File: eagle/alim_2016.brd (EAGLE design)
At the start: 160 x 100 mm, 22 parts, among them J1 AVR_SPI_PRG_6PTH, J2 AVR_SPI_PRG_6PTH, U1 3.3V, U2 LM2678S-5.0, U3 ATMEGA328P, U4 LM2596S-ADJ, U5 ATTINY85-20SU

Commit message: thermal vias
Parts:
- added 12V: 1751248, con-phoenix-350:1751248
- added R2, R3, R4, R5: 10K, resistor:M0805
- added S1, S2: (no value), SparkFun-Electromechanical:TACTILE-PTH
- moved J2 169.1 mm to (144.5, 48.6)
- moved U5 158.2 mm to (147.0, 44.1), turned to 180 degrees
- moved 24V 115.1 mm to (53.0, 29.8), turned to 0 degrees
- moved 8V 91.9 mm to (74.0, 29.8), turned to 0 degrees
- moved 5V 77.4 mm to (84.8, 29.8), turned to 0 degrees
- moved 3.3V 63.0 mm to (95.6, 29.8), turned to 0 degrees
- moved C2 57.3 mm to (88.6, 39.4), turned to 180 degrees
- moved U$20 56.8 mm to (40.6, 32.4), turned to 270 degrees
- moved U1 49.2 mm to (96.2, 40.0), turned to 180 degrees
- moved C3 48.7 mm to (51.8, 46.7), turned to 0 degrees
- moved C1 48.7 mm to (88.6, 47.6), turned to 180 degrees
- moved Q1 46.9 mm to (47.9, 43.2), turned to 0 degrees
- moved J1 43.3 mm to (48.6, 49.5)
- moved BAT1 42.5 mm to (13.3, 32.4)
- moved BAT2 42.5 mm to (13.3, 45.1)
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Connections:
- removed net N$38: 24V.1, U$20.3
- new net BAT24_CUT: R2.1, S2.3, U$20.1, U3.32
- new net N$12: 24V.1, BAT2.1, R3.1
- new net N$13: BAT3.2, R5.2, U$19.3
- new net N$15: R5.1, S1.1, U$19.1
- net 12V: now also 12V.1, BAT3.1, S1.3, U2.2; no longer U$19.3
- net GND: now also 12V.2, U$19.TAB, U$20.TAB; no longer BAT1.2, BAT3.2
- net N$8: now also BAT1.2, R2.2, R4.2, U$20.3; no longer BAT2.1, U$20.TAB
- net N$9: now also R3.2, R4.1, S2.1; no longer BAT3.1, U$19.TAB
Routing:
- net 12V: track 0.00 -> 163.2 mm, vias 0 -> 1
- net N$12: track 0.00 -> 59.7 mm
- net N$13: track 0.00 -> 18.3 mm
- net BAT24_CUT: track 0.00 -> 14.6 mm
- net N$42: track 0.00 -> 8.57 mm
- net N$40: track 0.00 -> 7.67 mm
- net N$41: track 0.00 -> 7.30 mm
- net N$8: track 14.9 -> 22.0 mm
- net 5.0V: track 40.6 -> 33.7 mm, vias 1 -> 3
- net N$6: track 12.6 -> 19.3 mm, vias 0 -> 1
- net N$39: track 0.00 -> 6.23 mm
- net N$15: track 0.00 -> 5.34 mm
- net N$2: track 13.3 -> 8.16 mm
- net RESET: track 19.0 -> 22.3 mm, vias 1 -> 2
- net N$3: track 5.67 -> 8.72 mm
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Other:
- board size 160 x 100 mm -> 160 x 67 mm

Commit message: pcb rearranging
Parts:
- removed U3: ATMEGA328P, SparkFun-DigitalIC:TQFP32-08
- added D1, D2: (no value), alim:SOD-123
- added LED1, LED4, LED7, LED8: RED, microbuilder:CHIPLED_0805_NOOUTLINE
- added LED2, LED5: YELLOW, microbuilder:CHIPLED_0805_NOOUTLINE
- added LED3, LED6: GREEN, microbuilder:CHIPLED_0805_NOOUTLINE
- added R10, R11, R12, R13, R6, R8, R9: 1K, resistor:M0805
- added R7: 220, resistor:M0805
- added U6: ATMEGA328P_TQFP, SparkFun-DigitalIC:TQFP32-08
- R3: value 10K -> 1K
- R4: value 10K -> 220
- S1, S2: value (none) -> SWITCH-MOMENTARY-2PTH
- moved C4 29.3 mm to (61.0, 17.8)
- moved Q1 29.3 mm to (67.0, 21.0)
- moved R1 29.3 mm to (47.0, 23.2)
- moved J1 29.3 mm to (67.6, 27.3)
- moved C3 29.3 mm to (70.8, 24.4)
- moved R4 18.3 mm to (32.7, 49.2), turned to 90 degrees
- moved 3.3V 11.2 mm to (96.8, 41.0)
- moved 5V 11.2 mm to (86.0, 41.0)
- moved C2 11.2 mm to (89.9, 50.5)
- moved 12V 11.2 mm to (64.8, 41.0)
- moved 24V 11.2 mm to (54.3, 41.0)
- moved 8V 11.2 mm to (75.2, 41.0)
- moved BAT1 11.2 mm to (14.6, 43.5)
- moved R2 11.2 mm to (31.1, 43.5)
- moved S1 11.2 mm to (25.4, 67.0)
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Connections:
- new net BAT12_CUT: D2.C, R5.1, R6.2, R7.1, S1.1, U$19.1
- new net N$10: LED7.A, R6.1
- new net N$11: R4.2, U6.32
- new net N$14: R7.2, U6.24
- new net N$16: LED5.A, R9.1
- new net N$17: LED6.A, R10.1
- new net N$18: LED1.A, R11.1
- new net N$19: LED2.A, R12.1
- new net N$20: LED3.A, R13.1
- net 5.0V: now also U6.4, U6.6; no longer U3.4, U3.6
- net BAT24_CUT: now also D1.C, R3.2, R4.1; no longer U3.32
- net GND: now also D1.A, D2.A, LED1.C, LED2.C, LED3.C, LED4.C, LED5.C, LED6.C, LED7.C, LED8.C, U6.3, U6.5; no longer U3.3, U3.5
- net N$12: no longer R3.1
- net N$15: now also LED4.A, R8.1; no longer R5.1, S1.1, U$19.1
- net N$2: now also U6.17; no longer U3.17
- net N$3: now also U6.16; no longer U3.16
- net N$4: now also U6.15; no longer U3.15
- net N$5: now also S2.1
- net N$6: now also U6.7; no longer U3.7
- net N$7: now also U6.8; no longer U3.8
- net N$8: no longer R4.2
- net N$9: now also LED8.A, R3.1; no longer R3.2, R4.1, S2.1
- net RESET: now also U6.29; no longer U3.29
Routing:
- net N$12: track 59.7 -> 47.4 mm
- net N$9: track 12.3 -> 2.13 mm
- net N$5: track 7.70 -> 16.5 mm
- net BAT12_CUT: track 0.00 -> 8.38 mm
- net 12V: track 163.2 -> 156.5 mm
- net BAT24_CUT: track 14.6 -> 8.26 mm
- net N$15: track 5.34 -> 0.00 mm
- net N$8: track 22.0 -> 18.8 mm
- net N$10: track 0.00 -> 1.81 mm
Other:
- board size 160 x 67 mm -> 105 x 105 mm

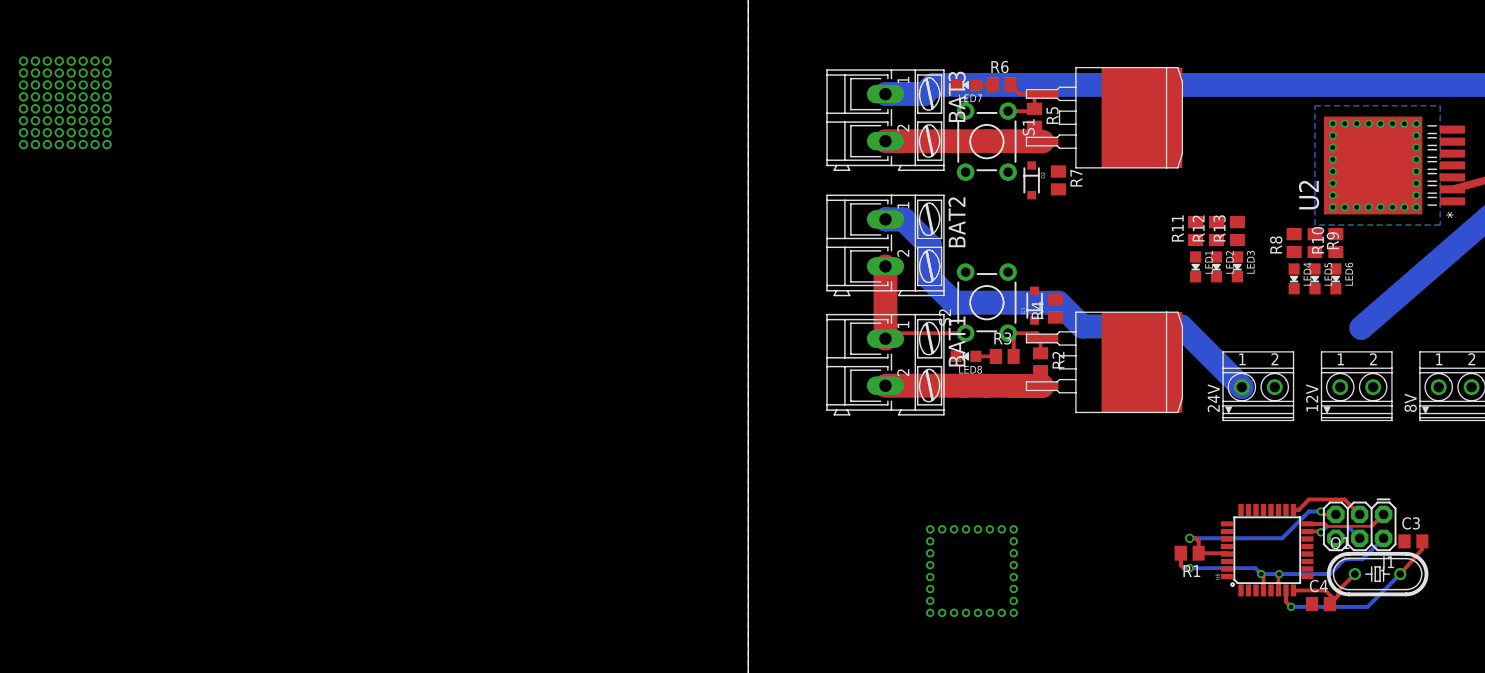
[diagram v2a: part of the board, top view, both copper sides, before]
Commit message: remove extra switch, routing
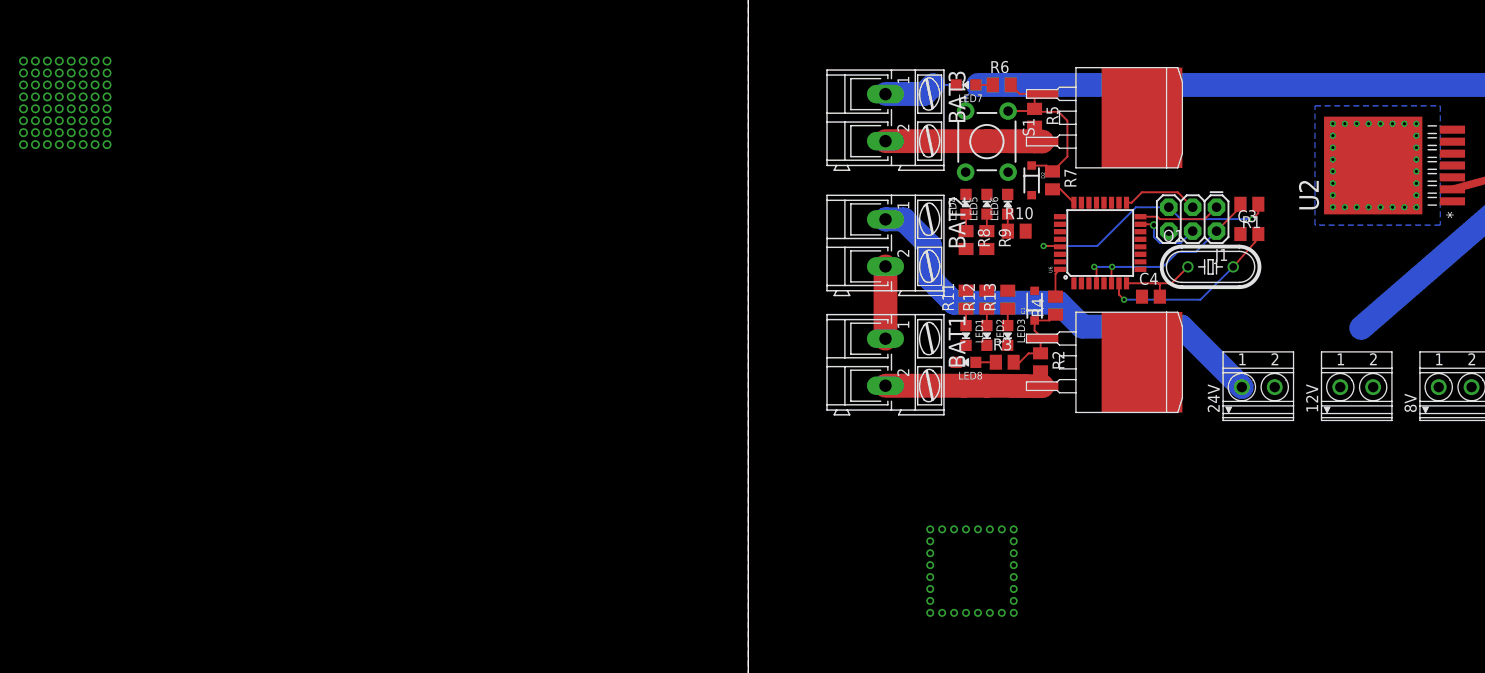
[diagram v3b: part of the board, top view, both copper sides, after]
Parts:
- removed S2: SWITCH-MOMENTARY-2PTH, SparkFun-Electromechanical:TACTILE-PTH
- moved R1 37.7 mm to (53.3, 60.3)
- moved C4 37.4 mm to (42.9, 50.5)
- moved J1 37.2 mm to (49.8, 60.0)
- moved Q1 37.2 mm to (49.2, 53.7)
- moved U6 37.2 mm to (37.5, 56.2)
- moved C3 37.1 mm to (53.3, 57.1)
- moved LED5 35.8 mm to (25.4, 60.3), turned to 0 degrees
- moved LED4 35.8 mm to (23.2, 60.3), turned to 0 degrees
- moved LED6 35.8 mm to (27.6, 60.3), turned to 0 degrees
- moved R9 34.9 mm to (25.4, 56.5)
- moved R8 34.9 mm to (23.2, 56.5), turned to 270 degrees
- moved R10 34.0 mm to (28.6, 57.5), turned to 0 degrees
- moved LED1 25.5 mm to (23.2, 46.4)
- moved LED3 25.5 mm to (27.6, 46.4)
- moved R11 25.5 mm to (23.2, 50.2)
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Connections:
- net BAT24_CUT: no longer S2.3
- net N$5: no longer S2.1
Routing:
- net BAT12_CUT: track 8.38 -> 21.0 mm
- net N$5: track 16.5 -> 8.52 mm
- net 5.0V: track 33.7 -> 27.4 mm, vias 3 -> 2
- net RESET: track 22.2 -> 28.1 mm
- net N$11: track 0.00 -> 3.11 mm
- net N$14: track 0.00 -> 2.87 mm
- net BAT24_CUT: track 8.26 -> 10.9 mm
- net N$16: track 0.00 -> 2.45 mm
- net N$20: track 0.00 -> 1.81 mm
- net N$19: track 0.00 -> 1.81 mm
- net N$18: track 0.00 -> 1.81 mm
- net N$17: track 0.00 -> 1.81 mm
- net N$15: track 0.00 -> 1.81 mm
- net N$4: track 6.62 -> 7.65 mm

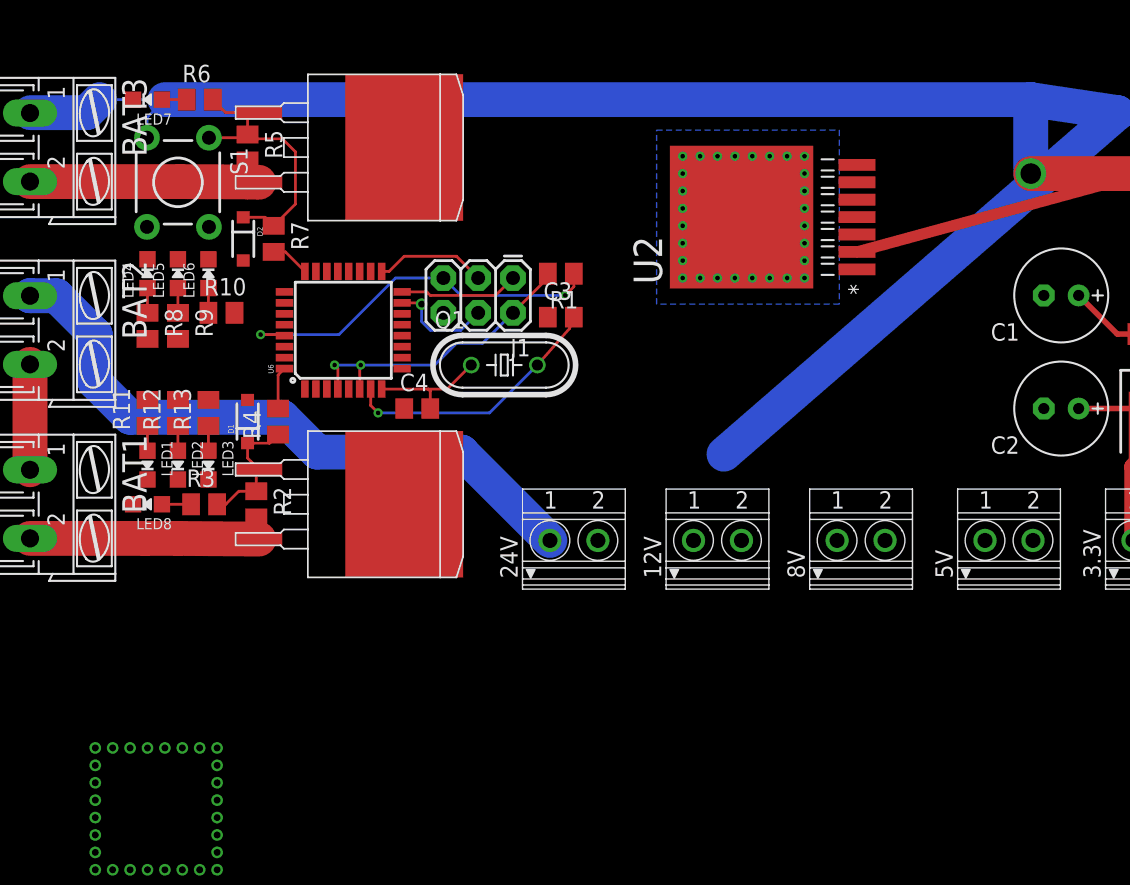
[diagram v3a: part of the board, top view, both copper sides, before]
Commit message: adding battery voltage sense
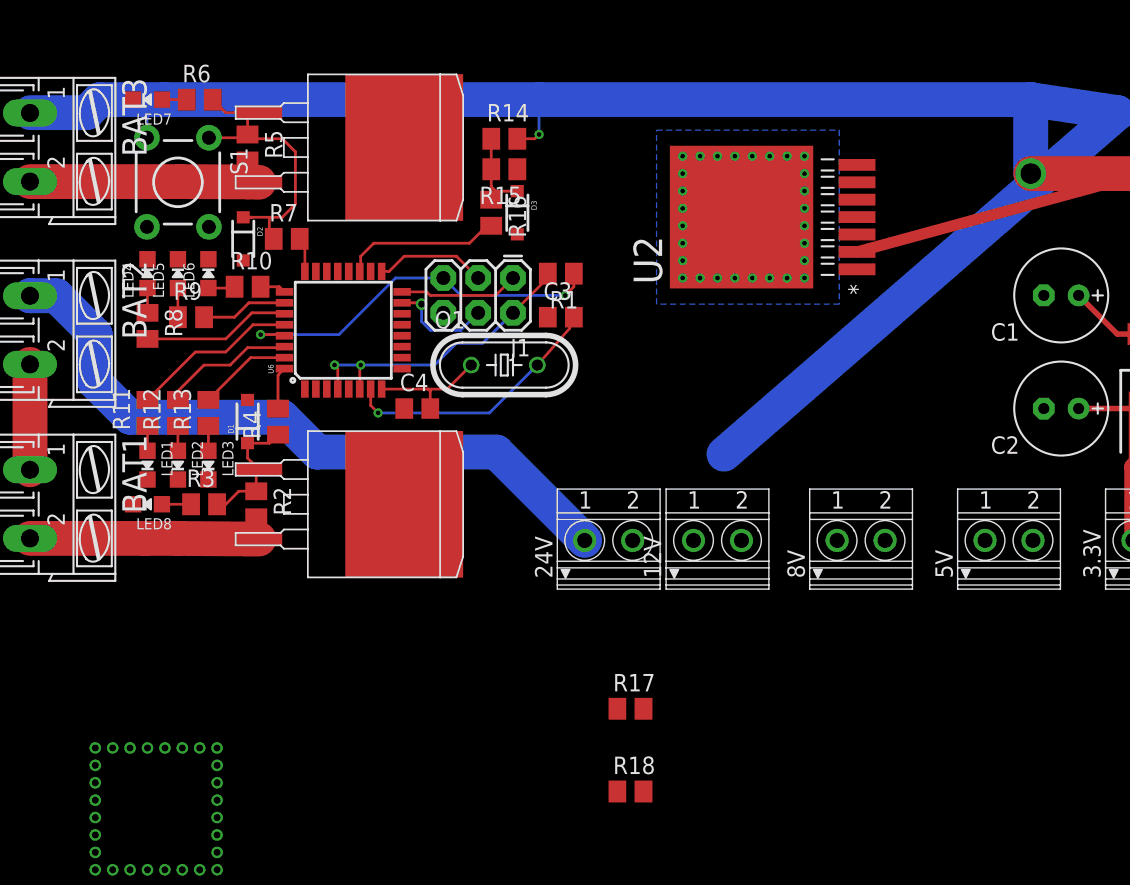
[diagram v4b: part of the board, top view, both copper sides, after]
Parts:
- added D3: (no value), alim:SOD-123
- added R14, R15, R17, R18: 1K, resistor:M0805
- added R16: 220, resistor:M0805
- moved R10 2.69 mm to (30.5, 59.4)
- moved 24V 2.54 mm to (56.8, 41.0)
- moved R9 1.14 mm to (26.4, 57.1), turned to 0 degrees
- moved R7 0.95 mm to (33.3, 62.9), turned to 0 degrees
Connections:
- new net BAT12_SENSE: D3.C, R14.1, R15.2, R16.1
- new net BAT24_SENSE: R17.1, R18.2
- new net N$21: R10.2, U6.25
- new net N$22: R9.2, U6.26
- new net N$23: R8.2, U6.27
- new net N$24: R13.2, U6.31
- new net N$25: R12.2, U6.30
- new net N$26: R11.2, U6.28
- new net N$27: R16.2, U6.19
- net 12V: now also R14.2
- net GND: now also D3.A, R15.1
- net N$12: now also R17.2
- net N$8: now also R18.1
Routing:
- net N$26: track 0.00 -> 12.3 mm
- net N$27: track 0.00 -> 11.6 mm
- net N$23: track 0.00 -> 10.8 mm
- net N$25: track 0.00 -> 9.75 mm
- net N$24: track 0.00 -> 6.83 mm
- net BAT12_SENSE: track 0.00 -> 6.49 mm
- net N$22: track 0.00 -> 6.30 mm
- net 12V: track 156.5 -> 160.8 mm, vias 1 -> 2
- net N$12: track 47.4 -> 50.0 mm
- net N$21: track 0.00 -> 1.98 mm
- net BAT12_CUT: track 21.0 -> 22.9 mm

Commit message: adding other battery voltage sense
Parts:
- added D4: (no value), alim:SOD-123
- added R19: 220, resistor:M0805
- moved R18 45.9 mm to (23.8, 52.7)
- moved R17 43.5 mm to (23.8, 54.9), turned to 180 degrees
- moved D1 5.26 mm to (35.7, 50.0), turned to 0 degrees
- moved R9 4.58 mm to (30.2, 59.7)
- moved R12 2.88 mm to (28.3, 50.5)
- moved R13 2.86 mm to (30.3, 49.2)
- moved R7 2.86 mm to (36.2, 62.9)
- moved R10 2.71 mm to (31.4, 61.9)
- moved D2 1.80 mm to (31.4, 64.1), turned to 180 degrees
- moved R8 0.90 mm to (23.8, 57.1), turned to 0 degrees
- moved R11 0.71 mm to (23.8, 49.8), turned to 0 degrees
- moved LED1 0.63 mm to (22.5, 46.4)
- moved LED2 0.63 mm to (24.8, 46.4)
- moved LED3 0.63 mm to (27.0, 46.4)
- moved LED4 0.63 mm to (22.5, 60.3)
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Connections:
- new net N$28: R19.2, U6.27
- net BAT24_SENSE: now also D4.C, R19.1
- net GND: now also D4.A
- net N$11: now also U6.2; no longer U6.32
- net N$14: now also R9.2; no longer R7.2
- net N$21: now also R8.2; no longer R10.2
- net N$22: now also R10.2, U6.23; no longer R9.2, U6.26
- net N$23: now also R7.2, U6.22; no longer R8.2, U6.27
- net N$24: now also U6.1; no longer U6.31
- net N$25: now also U6.32; no longer U6.30
- net N$26: now also U6.31; no longer U6.28
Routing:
- net N$8: track 18.8 -> 34.6 mm, vias 0 -> 1
- net N$12: track 50.0 -> 59.8 mm
- net N$23: track 10.8 -> 2.80 mm
- net N$21: track 1.98 -> 9.22 mm
- net BAT24_SENSE: track 0.00 -> 7.02 mm
- net N$28: track 0.00 -> 4.14 mm
- net N$25: track 9.75 -> 5.73 mm
- net N$16: track 2.57 -> 5.59 mm
- net N$19: track 1.81 -> 4.60 mm
- net BAT12_CUT: track 22.9 -> 20.7 mm
- net N$22: track 6.30 -> 4.19 mm
- net N$20: track 1.81 -> 3.69 mm
- net N$17: track 1.93 -> 3.72 mm
- net N$14: track 2.53 -> 3.88 mm
- net N$26: track 12.3 -> 11.2 mm
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
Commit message: clean up board
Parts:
- added C5: 10n, rcl:C0805
- added U$29: SRR1260, alim:12.5X12.5
- added U$30: SBRS8340, alim:SMC
- moved 12V 80.4 mm to (128.1, 90.5)
- moved 24V 80.4 mm to (120.2, 90.5)
- moved 3.3V 80.4 mm to (160.2, 90.5)
- moved 5V 80.4 mm to (149.4, 90.5)
- moved 8V 80.4 mm to (138.6, 90.5)
- moved C1 80.4 mm to (153.2, 108.3)
- moved C2 80.4 mm to (153.2, 100.0)
- moved U1 80.4 mm to (160.8, 100.6)
- moved U2 56.4 mm to (55.9, 9.05), turned to 180 degrees
- moved D2 35.8 mm to (25.4, 28.9)
- moved LED4 35.8 mm to (16.5, 25.1)
- moved LED5 35.8 mm to (18.7, 25.1)
- moved LED6 35.8 mm to (21.0, 25.1)
- moved LED7 35.8 mm to (17.1, 37.8)
- moved R1 35.8 mm to (47.3, 25.1)
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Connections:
- net N$12 renamed 24V
- new net N$29: C5.2, U$29.P$1, U$30.2, U2.1
- new net N$30: C5.1, U2.3
- net 5.0V: now also U$29.P$2, U2.6
- net GND: now also U$30.1
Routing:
- net 12V: track 160.8 -> 115.7 mm
- net N$29: track 0.00 -> 20.9 mm
- net 24V: track 59.8 -> 50.7 mm
- net 5.0V: track 27.4 -> 36.4 mm
- net N$30: track 0.00 -> 6.87 mm
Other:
- board size 105 x 105 mm -> 105.2 x 42.8 mm

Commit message: most of the circuit finished
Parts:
- 12V, 24V, 3.3V, 5V, 8V: value 1751248 -> MKDSN1,5/2-5,08; device con-phoenix-350:1751248 -> con-phoenix-508:MKDSN1,5/2-5,08
- moved 24V 136.9 mm to (13.3, 5.00)
- moved 12V 133.8 mm to (25.2, 4.92)
- moved 8V 132.7 mm to (37.1, 4.92)
- moved 5V 131.7 mm to (49.2, 4.92)
- moved 3.3V 130.8 mm to (61.3, 4.92)
- moved C2 113.0 mm to (78.0, 15.6)
- moved C1 113.0 mm to (78.0, 23.9)
- moved U1 113.0 mm to (85.7, 16.3)
- moved U4 71.5 mm to (74.0, 42.1)
- moved J2 65.6 mm to (84.4, 36.4)
- moved U5 65.6 mm to (86.9, 32.0)
- moved U$30 17.3 mm to (61.3, 42.5)
- moved U$29 16.2 mm to (52.0, 41.1)
- moved C5 15.8 mm to (60.9, 32.7)
- moved U2 15.8 mm to (54.8, 24.8)
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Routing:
- net 5.0V: track 36.4 -> 111.3 mm, vias 2 -> 3
- net N$1: track 15.9 -> 35.5 mm
- net 12V: track 115.7 -> 104.5 mm
- net 24V: track 50.7 -> 41.8 mm
- net N$29: track 20.9 -> 19.6 mm
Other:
- board size 105.2 x 42.8 mm -> 93.1 x 50.4 mm

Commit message: neater
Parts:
- moved U5 10.0 mm to (83.5, 22.6)
- moved J2 10.0 mm to (81.0, 27.1)
- moved U1 8.84 mm to (77.4, 13.1)
- moved C1 8.84 mm to (69.8, 20.7)
- moved C2 8.84 mm to (69.8, 12.4)
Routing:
- net N$1: track 35.5 -> 26.7 mm
- net 12V: track 104.5 -> 105.5 mm
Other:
- board size 93.1 x 50.4 mm -> 90 x 50 mm
